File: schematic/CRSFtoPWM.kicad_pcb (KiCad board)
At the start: 4 copper layers, 40 x 21 mm, 29 parts, among them J1 Bat+, J2 UART1/Rx, J3 ICSP, J4 TSW-104-08-G-T-RA, J5 TSW-104-08-G-T-RA, J6 TSW-104-08-G-T-RA, J7 TSW-102-08-L-T-RA, U1 AP7375-50W5-7, U2 AP2210N-3.3TRG1, U3 ATSAMD21E18A-MU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

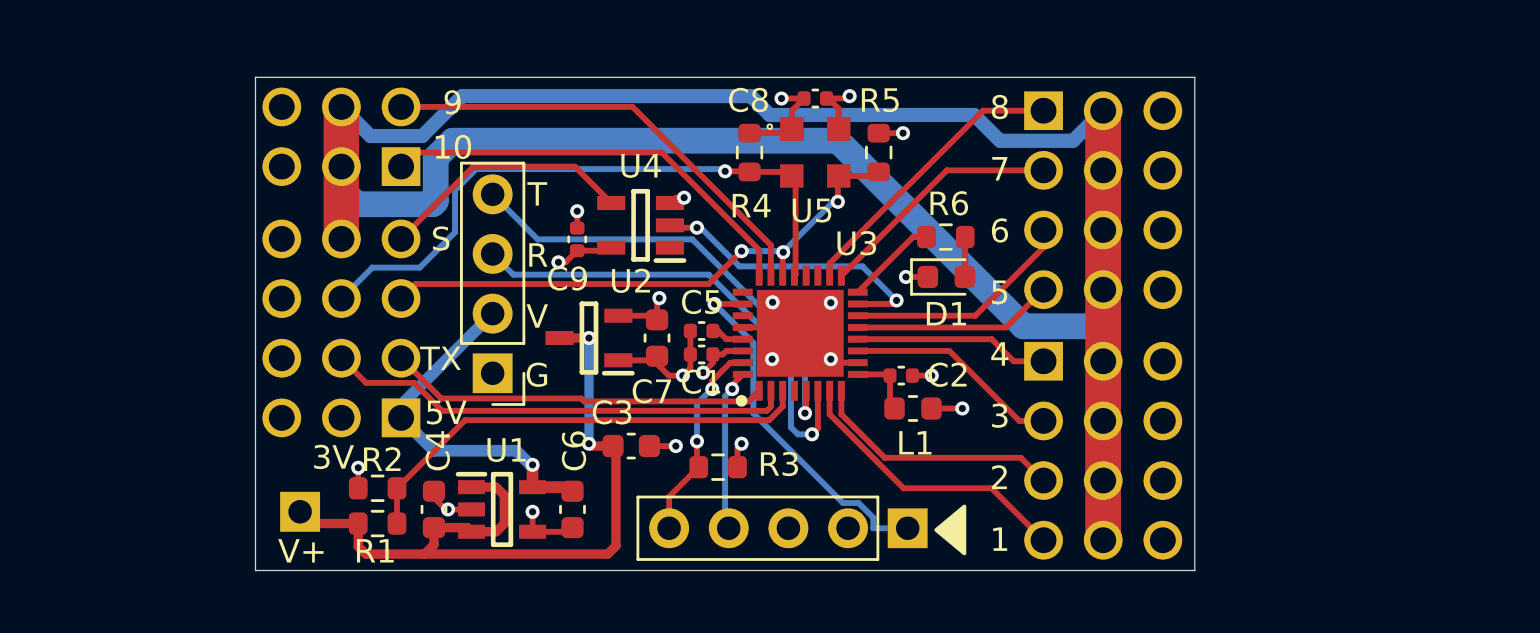
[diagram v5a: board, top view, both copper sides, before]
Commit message: Improved SCL,SDA traces
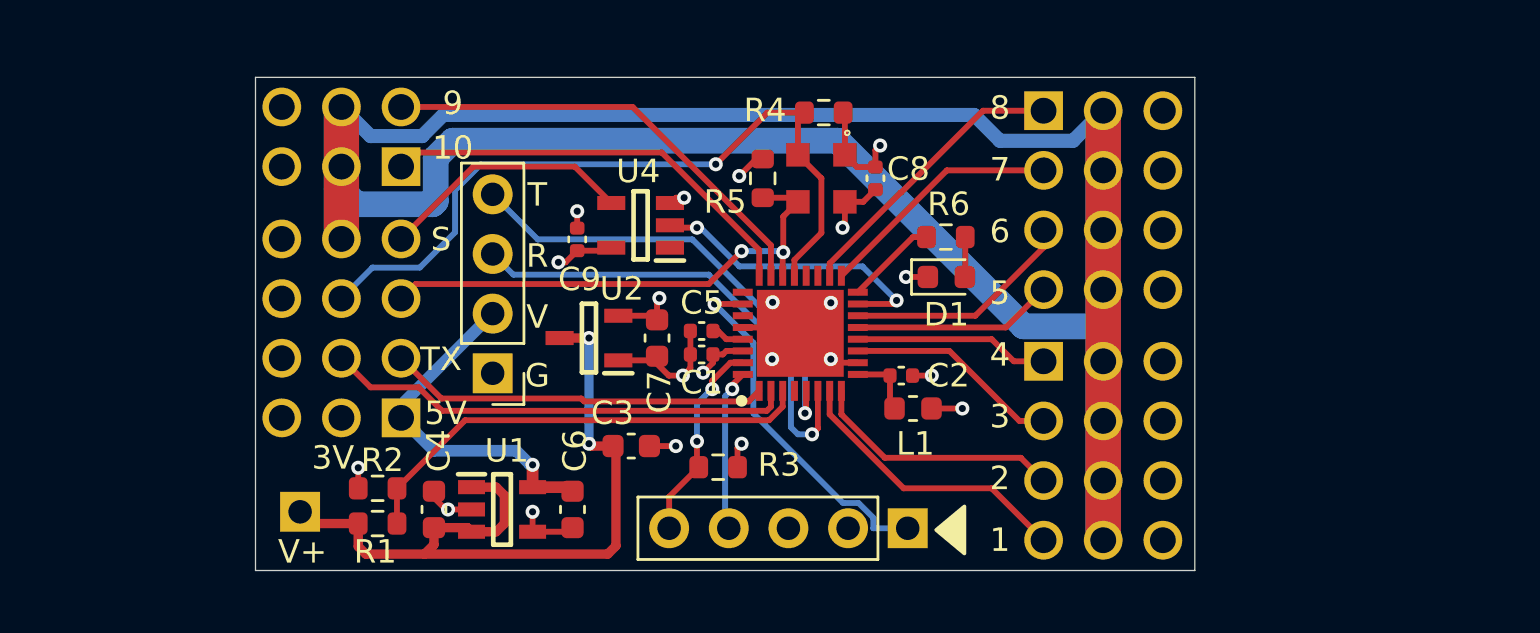
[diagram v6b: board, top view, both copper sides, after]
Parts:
- moved R5 5.06 mm to (162.6, 98.9)
- moved C8 4.26 mm to (167.4, 98.9), turned to -90 degrees
- moved R4 3.59 mm to (165.2, 96.1), turned to 180 degrees
- moved U5 1.13 mm to (165.1, 98.9), turned to -90 degrees
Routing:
- net SDA: track 26.4 -> 32.0 mm
- net SCL: track 24.0 -> 21.9 mm, vias 3 -> 2
- net Vservo: track 121.0 -> 120.3 mm
- net +3V3: track 14.6 -> 15.1 mm

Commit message: Added pullup to RESET
Updated pins in Harmony
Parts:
- added R7: 10K, Resistor_SMD:R_0603_1608Metric, F.Cu at (165.6, 111.2)
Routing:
- net Net-(J3-Pad1): track 15.0 -> 18.6 mm
- net +3V3: track 15.1 -> 17.9 mm
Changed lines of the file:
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@@
+    )
+  )
+  (footprint "Resistor_SMD:R_0603_1608Metric" (layer "F.Cu")
+    (at 165.6 111.2 180)
+    (descr "Resistor SMD 0603 (1608 Metric), square (rectangular) end terminal, IPC_7351 nominal, (Body size source: IPC-SM-782 page 72, https://www.pcb-3d.com/wordpress/wp-content/uploads/ipc-sm-782a_amendment_1_and_2.pdf), generated with kicad-footprint-generator")
+    (tags "resistor")
+    (property "Sheetfile" "CRSFtoPWM.kicad_sch")
+    (property "Sheetname" "")
+    (attr smd)
+    (fp_text reference "R7" (at -0.1 1.3) (layer "F.SilkS")
+      (effects (font (size 1 1) (thickness 0.15)))
+    )
+    (fp_text value "10K" (at 0 1.43) (layer "F.Fab")
+      (effects (font (size 1 1) (thickness 0.15)))
+    )
+    (fp_text user "${REFERENCE}" (at 0 0) (layer "F.Fab")
+      (effects (font (size 0.4 0.4) (thickness 0.06)))
+    )
+    (fp_line (start -0.237258 0.5225) (end 0.237258 0.5225) (layer "F.SilkS") (width 0.12))
+    (fp_line (start -0.237258 -0.5225) (end 0.237258 -0.5225) (layer "F.SilkS") (width 0.12))
+    (fp_line (start -1.48 -0.73) (end 1.48 -0.73) (layer "F.CrtYd") (width 0.05))
+    (fp_line (start 1.48 -0.73) (end 1.48 0.73) (layer "F.CrtYd") (width 0.05))
+    (fp_line (start 1.48 0.73) (end -1.48 0.73) (layer "F.CrtYd") (width 0.05))
+    (fp_line (start -1.48 0.73) (end -1.48 -0.73) (layer "F.CrtYd") (width 0.05))
+    (fp_line (start 0.8 0.4125) (end -0.8 0.4125) (layer "F.Fab") (width 0.1))
+    (fp_line (start -0.8 -0.4125) (end 0.8 -0.4125) (layer "F.Fab") (width 0.1))
+    (fp_line (start 0.8 -0.4125) (end 0.8 0.4125) (layer "F.Fab") (width 0.1))
+    (fp_line (start -0.8 0.4125) (end -0.8 -0.4125) (layer "F.Fab") (width 0.1))
+    (pad "1" smd roundrect (at -0.825 0 180) (size 0.8 0.95) (layers "F.Cu" "F.Paste" "F.Mask") (roundrect_rratio 0.25)
+      (net 36 "Net-(J3-Pad1)") (pintype "passive"))
+    (pad "2" smd roundrect (at 0.825 0 180) (size 0.8 0.95) (layers "F.Cu" "F.Paste" "F.Mask") (roundrect_rratio 0.25)
+      (net 1 "+3V3") (pintype "passive"))
+    (model "${KICAD6_3DMODEL_DIR}/Resistor_SMD.3dshapes/R_0603_1608Metric.wrl"
+      (offset (xyz 0 0 0))
+      (scale (xyz 1 1 1))
+      (rotate (xyz 0 0 0))
     )
   )
@@
   (segment (start 167.4 98.42) (end 166.62 98.42) (width 0.25) (layer "F.Cu") (net 1))
   (segment (start 161.525 110.375) (end 161.7 110.2) (width 0.25) (layer "F.Cu") (net 1))
+  (segment (start 164.775 112.34) (end 166.235 113.8) (width 0.25) (layer "F.Cu") (net 1))
   (segment (start 160.48 106.4) (end 160.9 106.4) (width 0.25) (layer "F.Cu") (net 1))
-  (segment (start 166.1 96.175) (end 166.025 96.1) (width 0.25) (layer "F.Cu") (net 1))
+  (segment (start 164.775 111.2) (end 164.775 112.34) (width 0.25) (layer "F.Cu") (net 1))
   (segment (start 156.45 104.75) (end 157.925 104.75) (width 0.25) (layer "F.Cu") (net 1))
   (segment (start 154.7 101.98) (end 154.204502 102.475498) (width 0.25) (layer "F.Cu") (net 1))
-  (segment (start 162.6 98.075) (end 162.325 98.075) (width 0.25) (layer "F.Cu") (net 1))
   (segment (start 161.525 111.2) (end 161.525 110.375) (width 0.25) (layer "F.Cu") (net 1))
   (segment (start 154.7 101.98) (end 156.02 101.98) (width 0.25) (layer "F.Cu") (net 1))
@@
   (segment (start 165.1 98.9) (end 164.1 97.9) (width 0.25) (layer "F.Cu") (net 34))
   (via (at 160.6 98.3) (size 0.6) (drill 0.3) (layers "F.Cu" "B.Cu") (net 34))
-  (segment (start 149.5 101.2) (end 149.5 99.4) (width 0.25) (layer "B.Cu") (net 34))
-  (segment (start 144.66 104.02) (end 145.98 102.7) (width 0.25) (layer "B.Cu") (net 34))
-  (segment (start 149.5 99.4) (end 150.6 98.3) (width 0.25) (layer "B.Cu") (net 34))
   (segment (start 150.6 98.3) (end 160.6 98.3) (width 0.25) (layer "B.Cu") (net 34))
   (segment (start 145.98 102.7) (end 148 102.7) (width 0.25) (layer "B.Cu") (net 34))
-  (segment (start 148 102.7) (end 149.5 101.2) (width 0.25) (layer "B.Cu") (net 34))
+  (segment (start 148 102.7) (end 149.7 101) (width 0.25) (layer "B.Cu") (net 34))
+  (segment (start 149.7 101) (end 149.7 99.2) (width 0.25) (layer "B.Cu") (net 34))
+  (segment (start 144.66 104.02) (end 145.98 102.7) (width 0.25) (layer "B.Cu") (net 34))
+  (segment (start 149.7 99.2) (end 150.6 98.3) (width 0.25) (layer "B.Cu") (net 34))
   (segment (start 163.4745 102.04708) (end 163.4745 100.5255) (width 0.25) (layer "F.Cu") (net 35))
   (segment (start 162.6 99.725) (end 163.925 99.725) (width 0.25) (layer "F.Cu") (net 35))
@@
   (segment (start 161.7 102) (end 163.42742 102) (width 0.25) (layer "B.Cu") (net 35))
   (segment (start 161.75 104.25) (end 160.55 104.25) (width 0.25) (layer "F.Cu") (net 36))
+  (segment (start 166.425 111.2) (end 166.425 111.45) (width 0.25) (layer "F.Cu") (net 36))
+  (segment (start 166.425 111.45) (end 168.775 113.8) (width 0.25) (layer "F.Cu") (net 36))
   (via (at 160.55 104.25) (size 0.6) (drill 0.3) (layers "F.Cu" "B.Cu") (net 36))
   (segment (start 167.31 113.35472) (end 167.31 113.8) (width 0.25) (layer "B.Cu") (net 36))

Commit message: Fixed JLC text
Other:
- board text added: "JLCJLCJLCJLC"
- board text removed: "JLCJLCJLC"
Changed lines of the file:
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@@
     (effects (font (size 1 1) (thickness 0.16)) (justify mirror))
   )
-  (gr_text "JLCJLCJLC" (at 149 114.7) (layer "B.SilkS")
+  (gr_text "JLCJLCJLCJLC" (at 149 114.7) (layer "B.SilkS")
     (effects (font (size 1 1) (thickness 0.16)) (justify mirror))
   )
@@
   (segment (start 168.98 107.3) (end 169.8 107.3) (width 0.25) (layer "F.Cu") (net 30))
   (segment (start 157.775 110.3) (end 158.9 110.3) (width 0.25) (layer "F.Cu") (net 30))
+  (segment (start 158.9 99.732916) (end 158.9 99.2) (width 0.25) (layer "F.Cu") (net 30))
   (segment (start 159.52 106.4) (end 159.52 105.4) (width 0.25) (layer "F.Cu") (net 30))
   (segment (start 159.52 106.98) (end 159.2 107.3) (width 0.25) (layer "F.Cu") (net 30))
@@
   (segment (start 166.1 99.9) (end 166.88 99.9) (width 0.25) (layer "F.Cu") (net 30))
   (segment (start 166.1 100.9) (end 166 101) (width 0.25) (layer "F.Cu") (net 30))
-  (segment (start 158.682916 99.95) (end 158.908416 99.7245) (width 0.25) (layer "F.Cu") (net 30))
+  (segment (start 158.682916 99.95) (end 158.9 99.732916) (width 0.25) (layer "F.Cu") (net 30))
   (segment (start 166.1 99.9) (end 166.1 100.9) (width 0.25) (layer "F.Cu") (net 30))
   (segment (start 158.6 107.3) (end 159.2 107.3) (width 0.25) (layer "F.Cu") (net 30))
-  (segment (start 158.908416 99.7245) (end 159.252537 99.7245) (width 0.25) (layer "F.Cu") (net 30))
   (segment (start 166.88 99.9) (end 167.4 99.38) (width 0.25) (layer "F.Cu") (net 30))
   (segment (start 149.1 113) (end 149.2 113) (width 0.25) (layer "F.Cu") (net 30))
@@
   (via (at 163 106.6) (size 0.6) (drill 0.3) (layers "F.Cu" "B.Cu") (net 30))
   (via (at 165.5 104.2) (size 0.6) (drill 0.3) (layers "F.Cu" "B.Cu") (net 30))
-  (via (at 159.252537 99.7245) (size 0.6) (drill 0.3) (layers "F.Cu" "B.Cu") (net 30))
+  (via (at 158.9 99.2) (size 0.6) (drill 0.3) (layers "F.Cu" "B.Cu") (net 30))
   (via (at 149.2 113) (size 0.6) (drill 0.3) (layers "F.Cu" "B.Cu") (net 30))
   (via (at 163.020878 104.179122) (size 0.6) (drill 0.3) (layers "F.Cu" "B.Cu") (net 30))
